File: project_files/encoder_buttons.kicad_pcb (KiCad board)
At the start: 2 copper layers, 36 parts, among them J1 Conn_01x08, J2 Conn_01x08, SW1 A, SW2 EC11, SW3 C, SW5 E, U1 74HC14

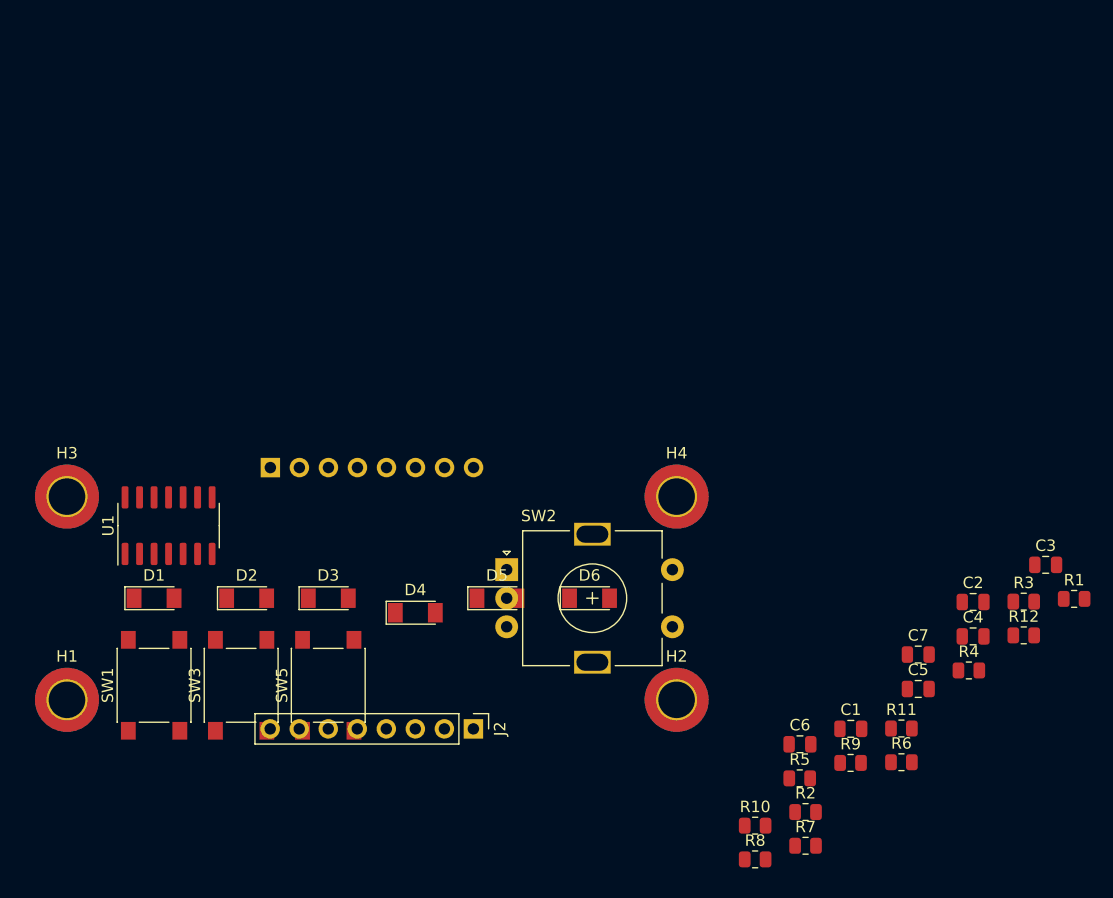
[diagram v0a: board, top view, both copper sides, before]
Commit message: Reopened in Kicad 8
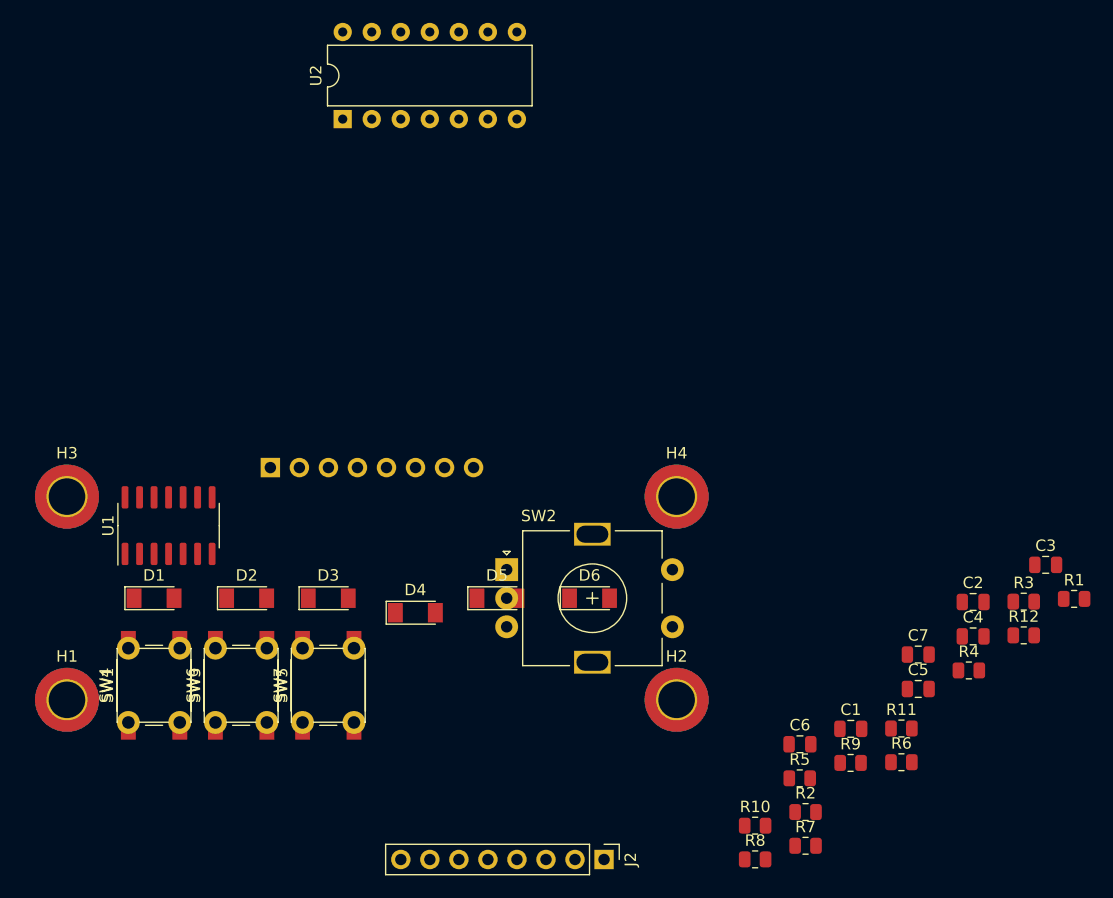
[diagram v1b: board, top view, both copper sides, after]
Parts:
- added SW4: A, Button_Switch_THT:SW_PUSH_6mm, F.Cu at (87.9, 94.7)
- added SW6: B, Button_Switch_THT:SW_PUSH_6mm, F.Cu at (95.5, 94.7)
- added SW7: C, Button_Switch_THT:SW_PUSH_6mm, F.Cu at (103.2, 94.7)
- added U2: 74HC14, Package_DIP:DIP-14_W7.62mm, F.Cu at (106.7, 41.9)
- SW3: value C -> B
- SW5: value E -> C
- moved J2 16.2 mm to (129.5, 106.7)
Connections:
- net Net-(C1-Pad1) renamed /BUT_A
- net Net-(C2-Pad1) renamed /ENC_C
- net Net-(C3-Pad1) renamed /BUT_B
- net Net-(C4-Pad1) renamed /ENC_B
- net Net-(C5-Pad1) renamed /BUT_C
- net Net-(C6-Pad1) renamed /ENC_A

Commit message: placing the components
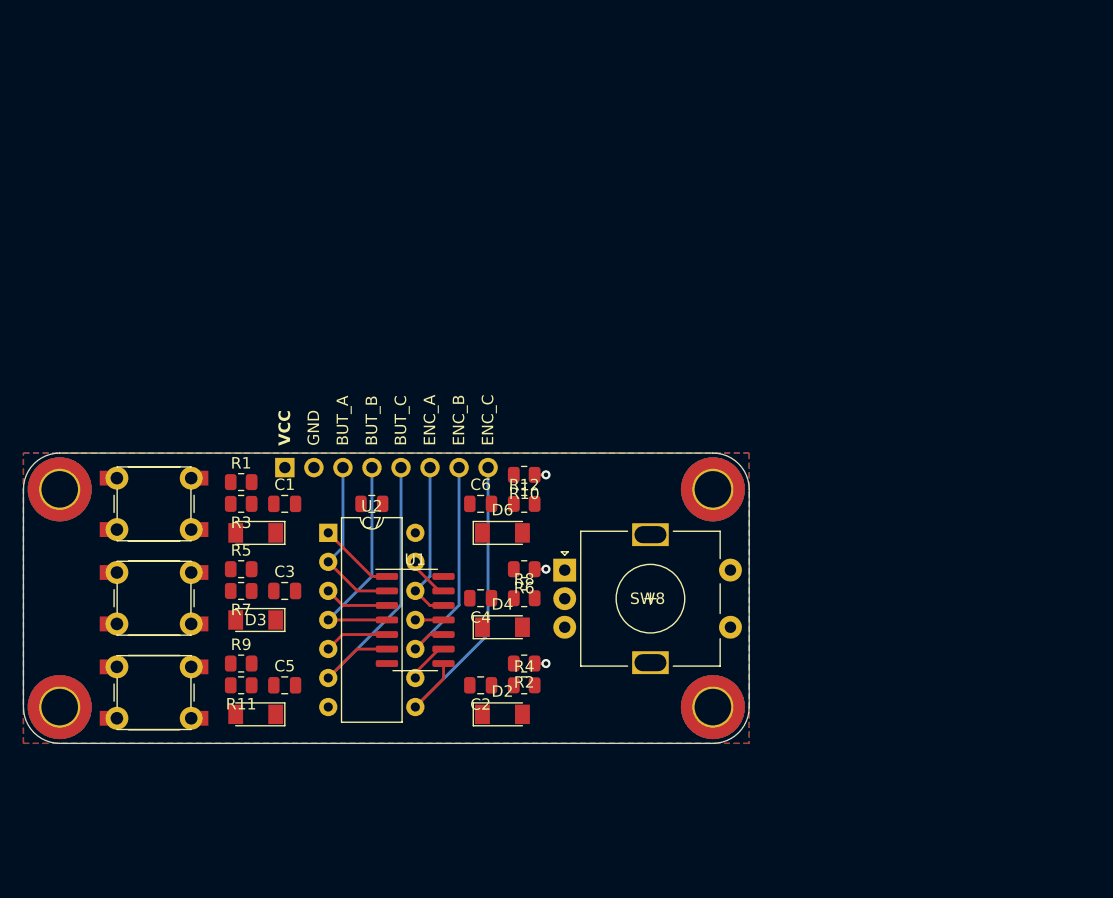
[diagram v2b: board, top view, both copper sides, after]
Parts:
- removed J2: Conn_01x08, Connector_PinHeader_2.54mm:PinHeader_1x08_P2.54mm_Vertical
- removed SW2: EC11, Rotary_Encoder:RotaryEncoder_Alps_EC11E-Switch_Vertical_H20mm
- added SW8: EC11, Rotary_Encoder:RotaryEncoder_Alps_EC11E-Switch_Vertical_H20mm, F.Cu at (126.1, 81.4)
- J1: value Conn_01x08 -> UPPER
- moved R1 73.6 mm to (97.8, 73.7)
- moved R3 69.0 mm to (97.8, 75.6), turned to 180 degrees
- moved C3 66.6 mm to (101.6, 83.2)
- moved R11 57.9 mm to (97.8, 91.4), turned to 180 degrees
- moved C5 55.4 mm to (101.6, 91.4)
- moved R7 54.2 mm to (97.8, 83.2), turned to 180 degrees
- moved R9 54.0 mm to (97.8, 89.5)
- moved C1 53.3 mm to (101.6, 75.6)
- moved R5 52.2 mm to (97.8, 81.3)
- moved C7 49.6 mm to (109.2, 75.6), turned to 180 degrees
- moved R12 45.2 mm to (122.6, 75.6)
- moved C2 43.7 mm to (118.7, 91.4), turned to 180 degrees
- moved C4 43.2 mm to (118.7, 83.8), turned to 180 degrees
- moved R4 38.9 mm to (122.6, 91.4)
- moved R6 37.1 mm to (122.6, 81.3), turned to 180 degrees
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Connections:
- U1 pad 10: BUTTON_C -> ENCODER_B
- U1 pad 11: /BUT_C -> /ENC_B
- U1 pad 3: /ENC_C -> /BUT_B
- U1 pad 4: ENCODER_SW -> BUTTON_B
- U1 pad 5: /BUT_B -> /BUT_C
- U1 pad 6: BUTTON_B -> BUTTON_C
- U1 pad 8: ENCODER_B -> ENCODER_SW
- U1 pad 9: /ENC_B -> /ENC_C
- U2 pad 10: BUTTON_C -> ENCODER_B
- U2 pad 11: /BUT_C -> /ENC_B
- U2 pad 3: /ENC_C -> /BUT_B
- U2 pad 4: ENCODER_SW -> BUTTON_B
- U2 pad 5: /BUT_B -> /BUT_C
- U2 pad 6: BUTTON_B -> BUTTON_C
- U2 pad 8: ENCODER_B -> ENCODER_SW
- U2 pad 9: /ENC_B -> /ENC_C
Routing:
- net ENCODER_SW: track 0.00 -> 28.4 mm
- net BUTTON_C: track 0.00 -> 27.2 mm
- net ENCODER_B: track 0.00 -> 20.4 mm
- net BUTTON_B: track 0.00 -> 20.1 mm
- net BUTTON_A: track 0.00 -> 15.0 mm
- net ENCODER_A: track 0.00 -> 14.3 mm
- net /BUT_A: track 0.00 -> 6.72 mm
- net /BUT_B: track 0.00 -> 5.66 mm
- net /BUT_C: track 0.00 -> 5.66 mm
- net /ENC_A: track 0.00 -> 3.79 mm
- net /ENC_C: track 0.00 -> 3.78 mm
- net VCC: track 0.00 -> 2.98 mm, vias 0 -> 3
- net /ENC_B: track 0.00 -> 2.47 mm
- added copper zone on B.Cu, net GND
- added copper zone on F.Cu, net GND
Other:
- board outline added: 63.5 x 25.4 mm
- board text added: "BUT_A"
- board text added: "BUT_B"
- board text added: "BUT_C"
- board text added: "ENC_A"
- board text added: "ENC_B"
- board text added: "ENC_C"
- board text added: "GND"
- board text added: "VCC"
